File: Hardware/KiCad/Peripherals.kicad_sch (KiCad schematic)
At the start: 69 parts

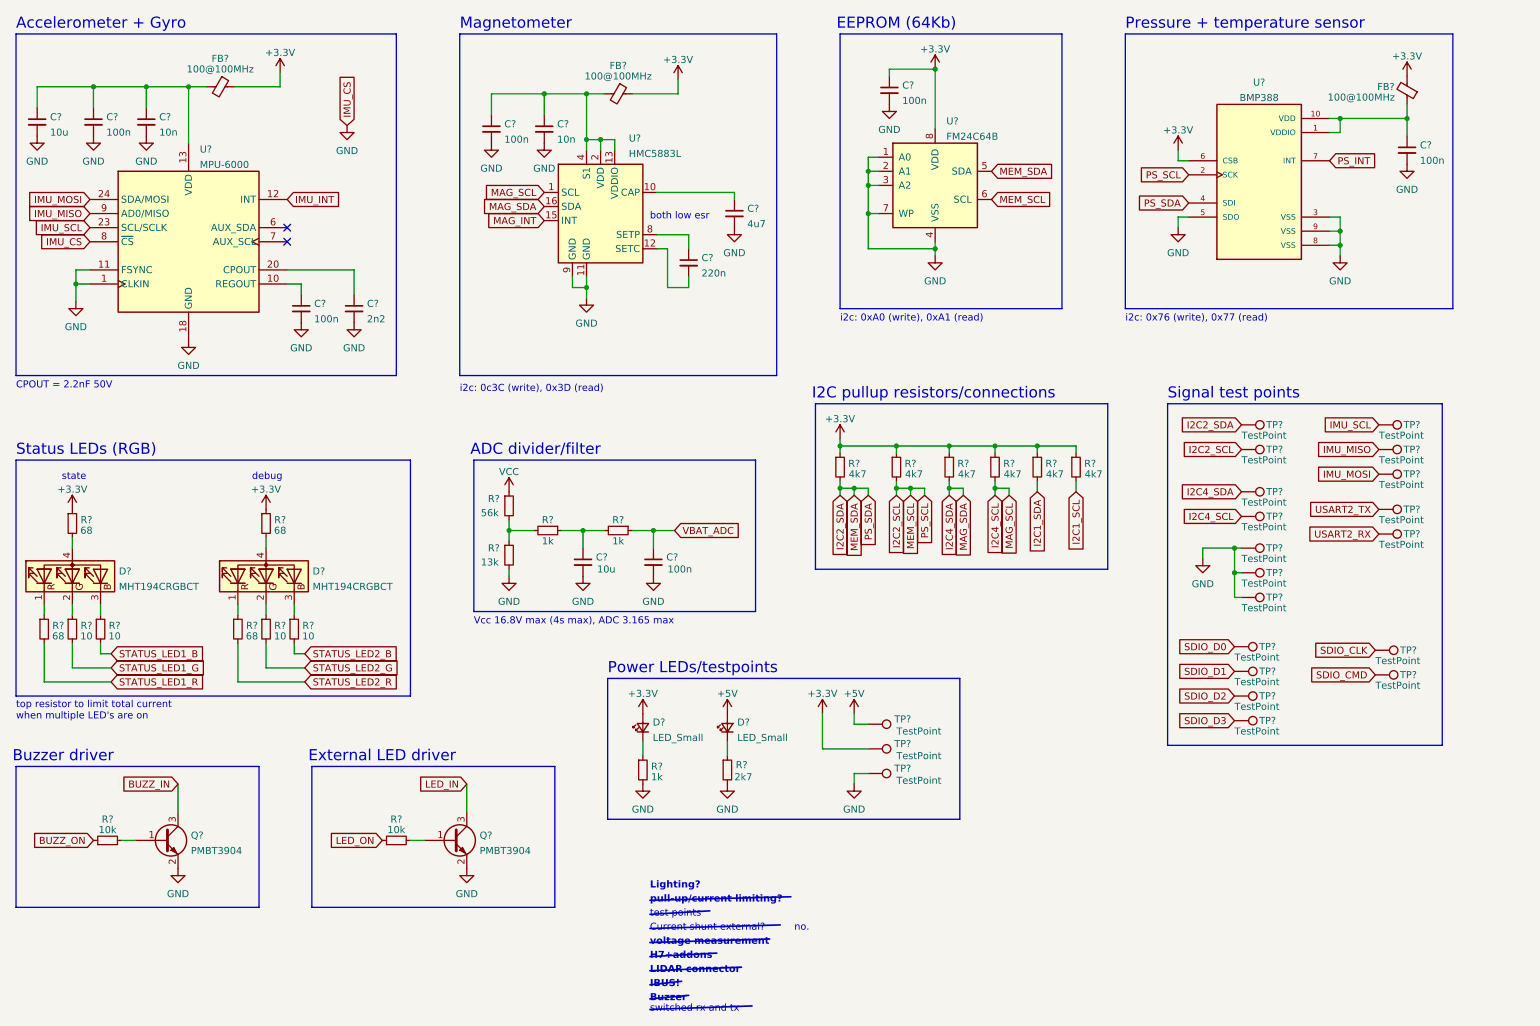
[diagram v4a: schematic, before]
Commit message: Fixed duplicate external LED driver
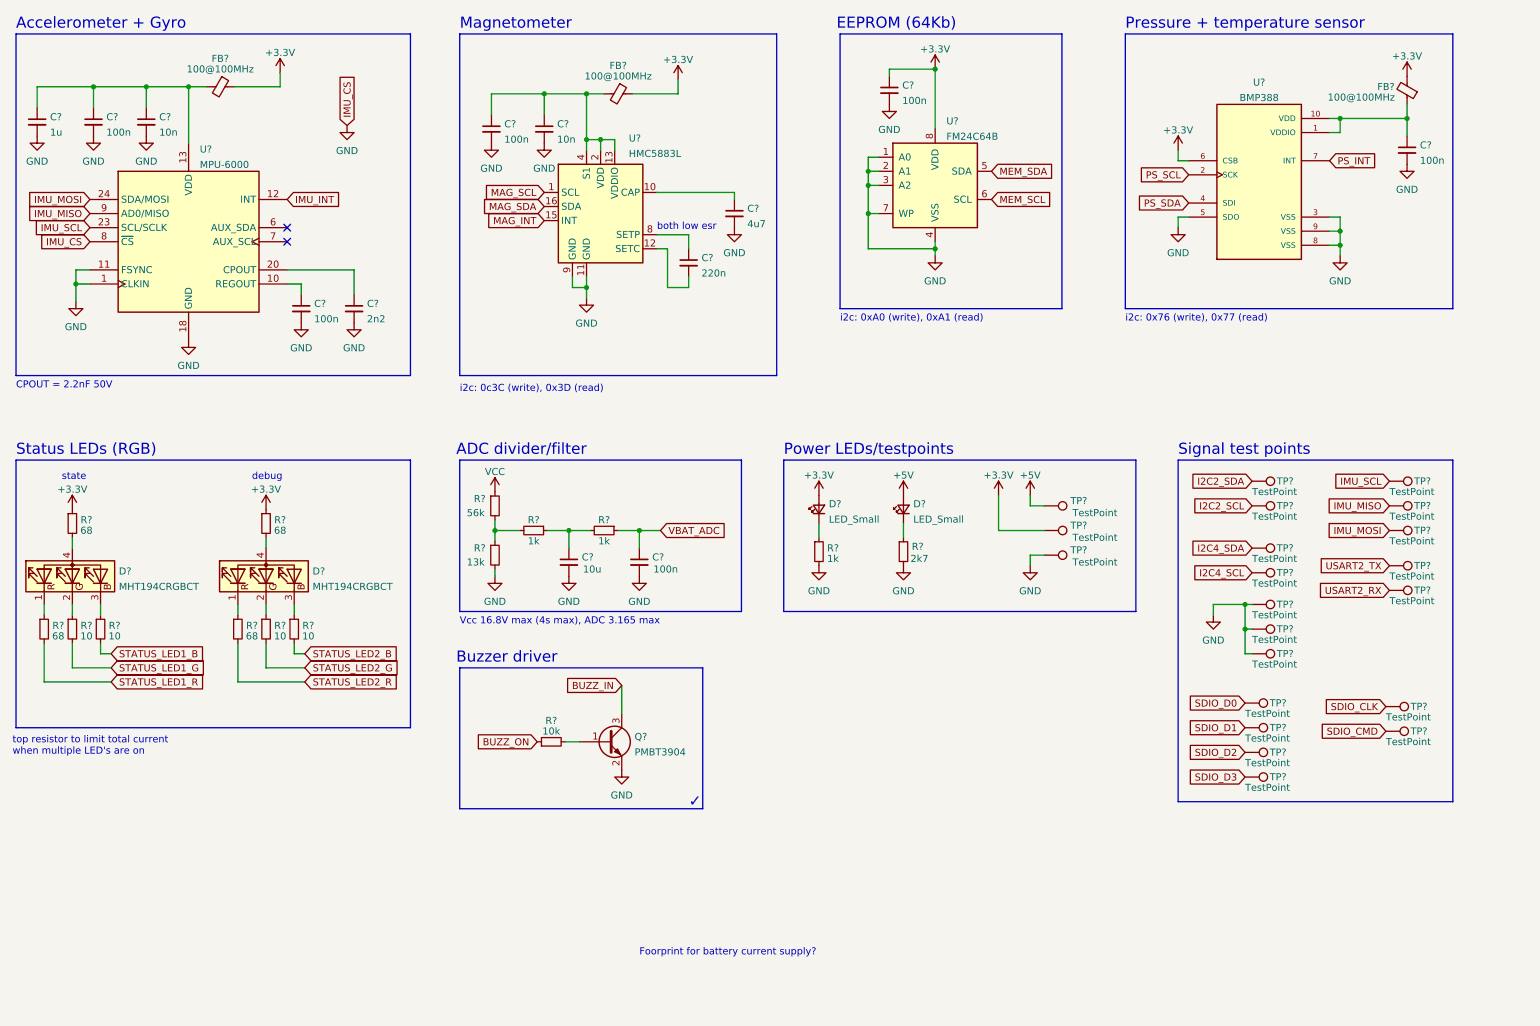
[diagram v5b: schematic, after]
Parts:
- removed Q?: PMBT3904, Package_TO_SOT_SMD:SOT-23, symbol Device:Q_NPN_BEC
- removed R?: 10k, Resistor_SMD:R_0402_1005Metric, symbol Device:R_Small
- removed R? (x6): 4k7, Resistor_SMD:R_0402_1005Metric, symbol Device:R_Small
- C?: value 10u -> 1u
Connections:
- net I2C2_SCL: no longer U?.2 (SCK), U?.6 (SCL)
- net I2C2_SDA: no longer U?.4 (SDI), U?.5 (SDA)
- net I2C4_SCL: no longer U?.1 (SCL)
- net I2C4_SDA: no longer U?.16 (SDA)
- new net MAG_SCL: U?.1 (SCL)
- new net MAG_SDA: U?.16 (SDA)
- new net MEM_SCL: U?.6 (SCL)
- new net MEM_SDA: U?.5 (SDA)
- new net PS_SCL: U?.2 (SCK)
- new net PS_SDA: U?.4 (SDI)
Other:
- note added: "Foorprint for battery current supply?"
- note added: "✓"
- note removed: "Buzzer"
- note removed: "Current shunt external?"
- note removed: "External LED driver"
- note removed: "H7+addons"
- note removed: "I2C pullup resistors/connections"
- note removed: "IBUS!"
- note removed: "LIDAR connector"
- note removed: "Lighting?"
- note removed: "no."
- note removed: "pull-up/current limiting?"
- note removed: "switched rx and tx"
- note removed: "test points"
- note removed: "voltage measurement"
- moved on the sheet: C?, D?, Q?, R?, TP?

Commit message: Added a footprint for an optional VBAT->5V regulator
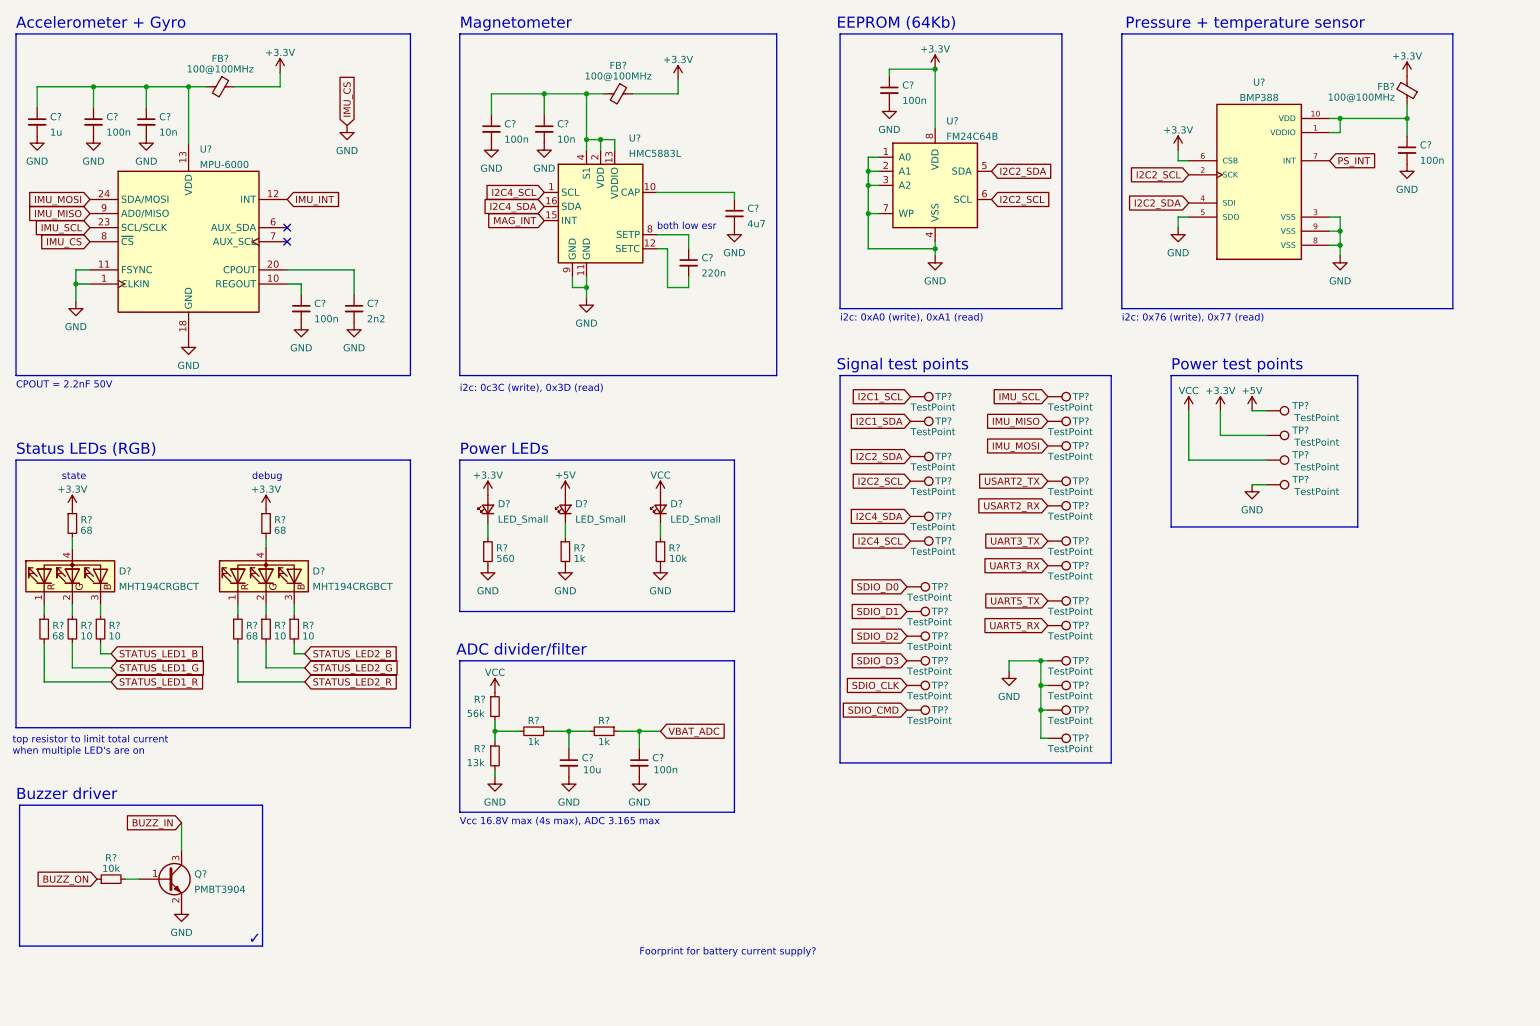
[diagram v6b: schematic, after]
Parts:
- removed R?: 2k7, Resistor_SMD:R_0603_1608Metric, symbol Device:R_Small
- removed R?: 1k, Resistor_SMD:R_0603_1608Metric, symbol Device:R_Small
- added D?: LED_Small, LED_SMD:LED_0603_1608Metric, symbol Device:LED_Small
- added R?: 560, Resistor_SMD:R_0603_1608Metric, symbol Device:R_Small
- added R?: 1k, Resistor_SMD:R_0603_1608Metric, symbol Device:R_Small
- added R?: 10k, Resistor_SMD:R_0603_1608Metric, symbol Device:R_Small
- added TP? (x8): TestPoint, TestPoint:TestPoint_Pad_D1.5mm, symbol Connector:TestPoint
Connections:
- net MAG_SCL is gone; now on net I2C4_SCL: U?.1 (SCL)
- net MAG_SDA is gone; now on net I2C4_SDA: U?.16 (SDA)
- net MEM_SCL is gone; now on net I2C2_SCL: U?.6 (SCL)
- net MEM_SDA is gone; now on net I2C2_SDA: U?.5 (SDA)
- net PS_SCL is gone; now on net I2C2_SCL: U?.2 (SCK)
- net PS_SDA is gone; now on net I2C2_SDA: U?.4 (SDI)
- net GND: now also R?.2, R?.2, R?.2, TP?.1
- net VCC: now also D?.2 (A), TP?.1
- net at D?.1 (K): now also R?.1 (x2)
- new net: D?.1 (K), R?.1
- new net I2C1_SCL: TP?.1
- new net I2C1_SDA: TP?.1
- new net UART3_RX: TP?.1
- new net UART3_TX: TP?.1
- new net UART5_RX: TP?.1
- new net UART5_TX: TP?.1
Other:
- note added: "Power LEDs"
- note added: "Power test points"
- note removed: "Power LEDs/testpoints"
- moved on the sheet: C?, D?, Q?, R?, TP?

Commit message: Final schematic changes made, added some annotations
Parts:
- removed C?: 10u, Capacitor_SMD:C_0603_1608Metric, symbol Device:C_Small
- added C? (x2): 100n, Capacitor_SMD:C_0402_1005Metric, symbol Device:C_Small
- added TP? (x2): TestPoint, TestPoint:TestPoint_Pad_D1.5mm, symbol Connector:TestPoint
- C?: value 100n -> 10n
- R? (x2): value 68 -> 220
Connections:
- net GND: now also C?.2, C?.2, TP?.1, TP?.1; no longer U?.7 (WP)
- net at C?.1, FB?.1, U?.1 (VDDIO)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: now also C?.1
- net at R?.1, R?.2: now also C?.1
- no-connect marks 2 -> 3
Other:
- note added: "Be mindfull of the keepout area"
- note added: "Maybe some GPIOs?"
- note added: "SCL"
- note added: "SDA"
- note added: "i2c: 0x76 (write), 0x77 (read), CSB selects I2C"
- note removed: "Foorprint for battery current supply?"
- note removed: "i2c: 0x76 (write), 0x77 (read)"
- moved on the sheet: C?, D?, FB?, R?, TP?, U?

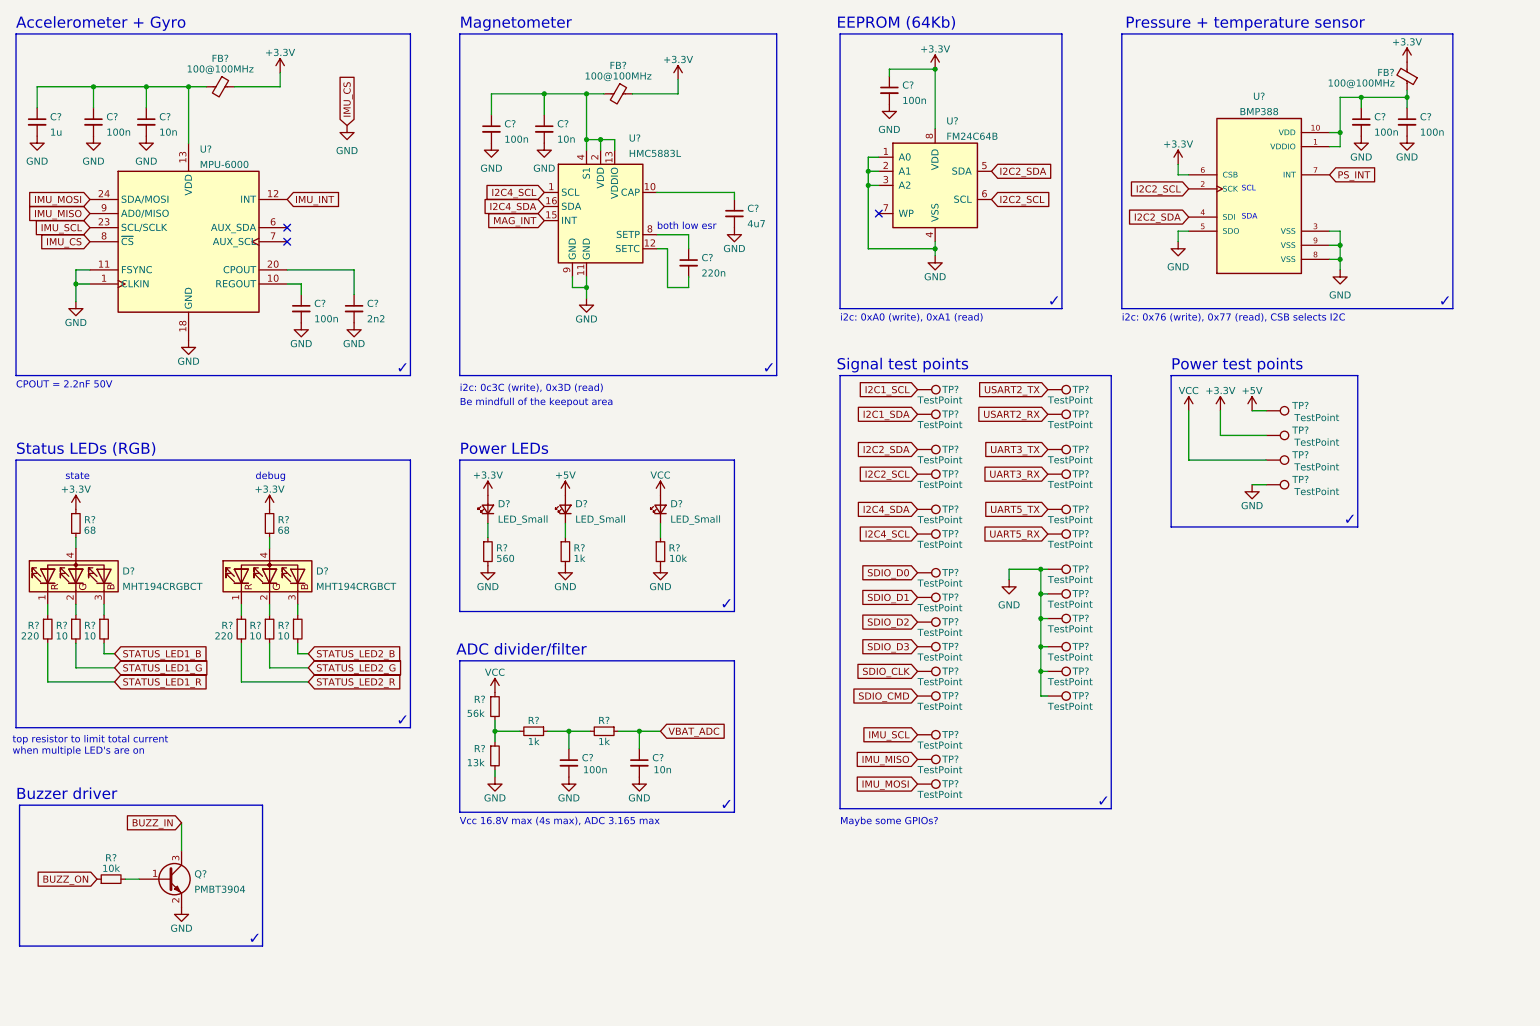
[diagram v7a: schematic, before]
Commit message: Fixed ERC errors
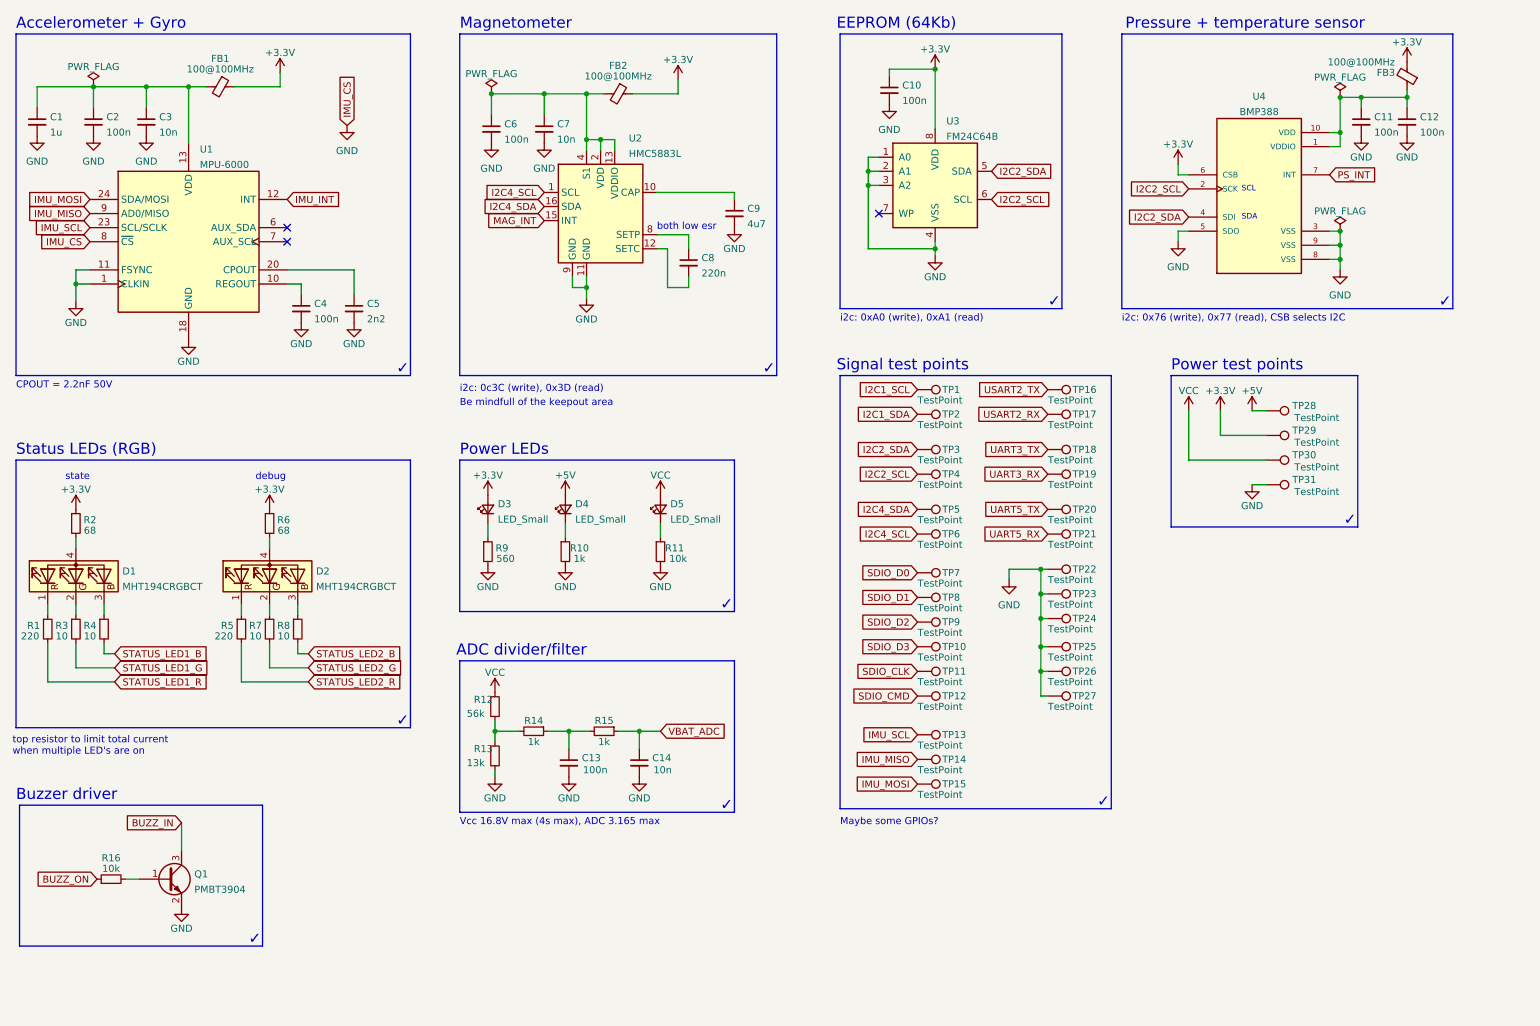
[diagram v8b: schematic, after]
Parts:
- gave numbers to parts that had none: 74
